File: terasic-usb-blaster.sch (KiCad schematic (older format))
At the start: 12 parts, among them J2 JTAG/AS/PS, J3 USB_B, U1 FT245BL, U3 Microchip 93LC46B, X1 6MHz, Y1 MCE AD8BB 24.000

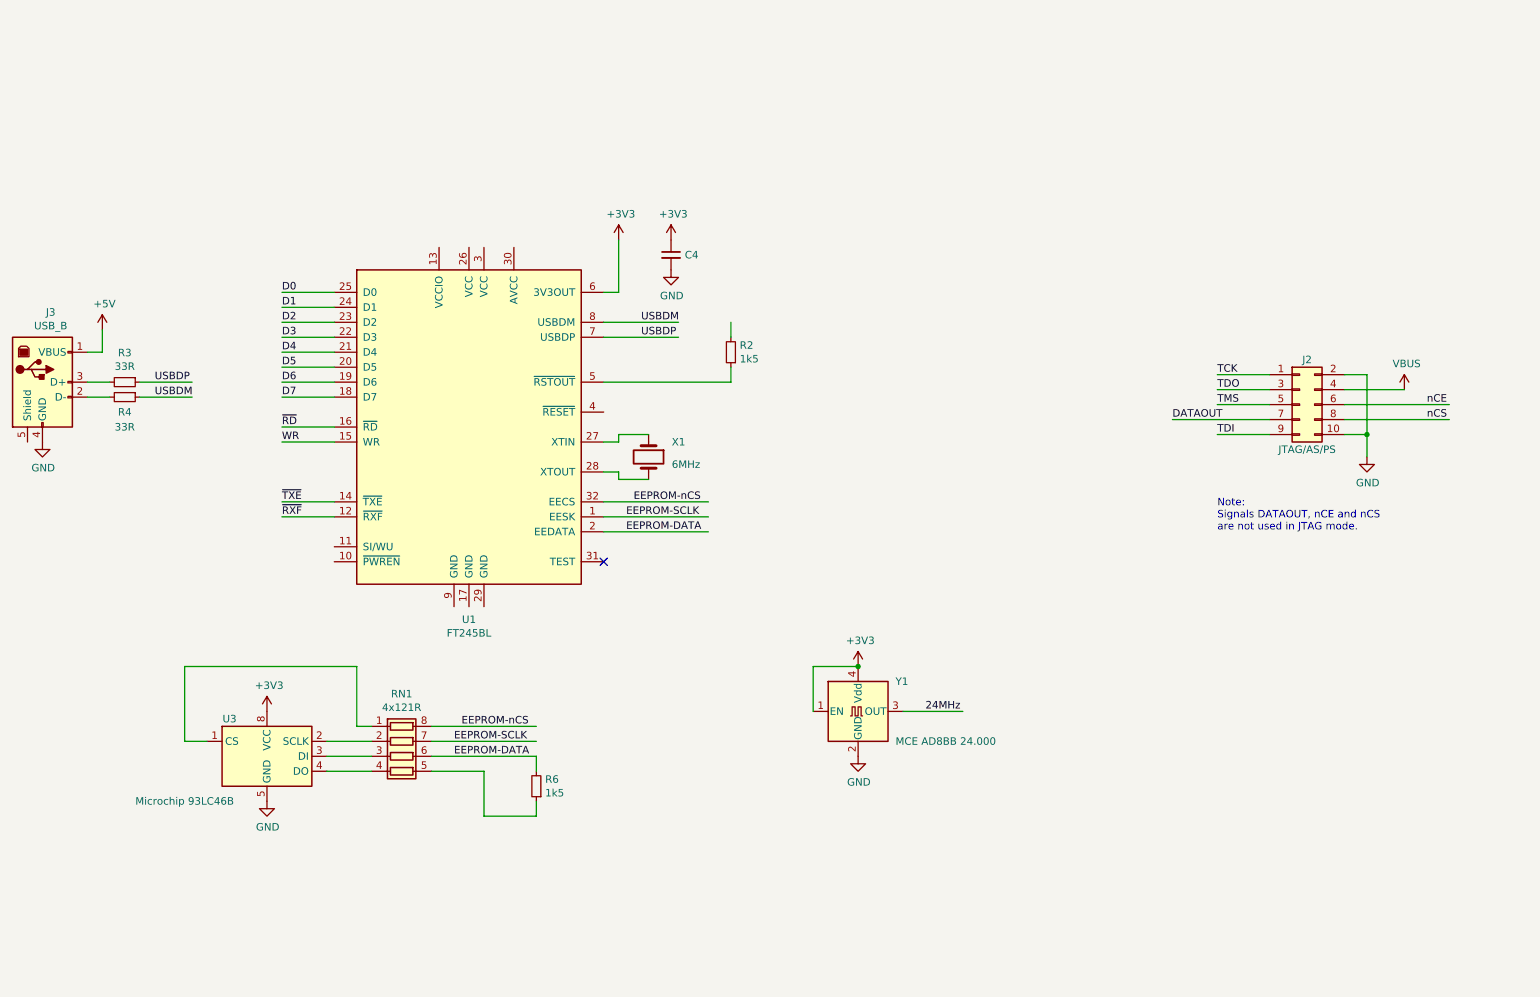
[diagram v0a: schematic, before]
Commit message: Added CPLD and level shifter
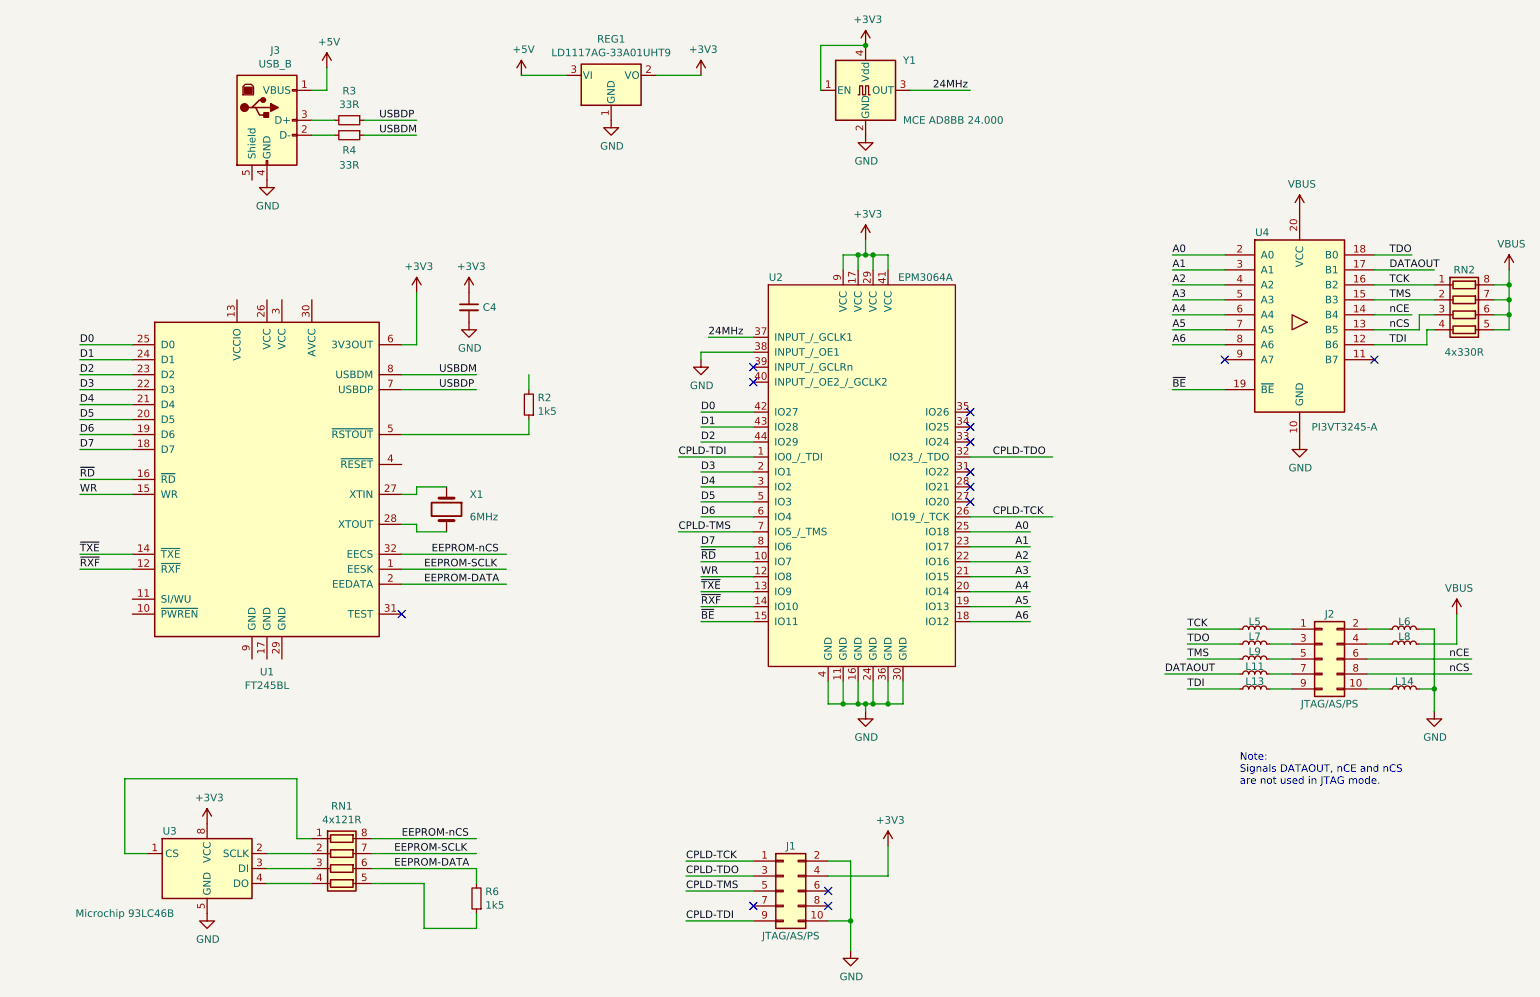
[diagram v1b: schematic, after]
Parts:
- added J1: JTAG/AS/PS, symbol Connector_Generic:Conn_02x05_Odd_Even
- added L11, L13, L14, L5, L6, L7, L8, L9: L_Small, symbol Device:L_Small
- added REG1: LD1117AG-33A01UHT9, Package_TO_SOT_SMD:SOT-223-3_TabPin2, symbol Regulator_Linear:LD1117S33TR_SOT223
- added RN2: 4x330R, symbol Device:R_Pack04
- added U2: EPM3064A, symbol Matthias:EPM3064A
- added U4: PI3VT3245-A, symbol Matthias:PI3VT3245-A
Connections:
- net labels added: A0, A1, A2, A3, A4, A5, A6, CPLD-TCK, CPLD-TDI, CPLD-TDO, CPLD-TMS, ~BE
- wire segments 65 -> 162
- no-connect marks 1 -> 14
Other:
- moved on the sheet: C4, J2, J3, R2, R3, R4, R6, RN1, U1, U3, X1, Y1
